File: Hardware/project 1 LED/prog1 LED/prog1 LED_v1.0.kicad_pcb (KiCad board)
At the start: 2 copper layers, 16.2 x 22 mm, 6 parts, among them J1 Conn_01x02, SW1 SW_Push

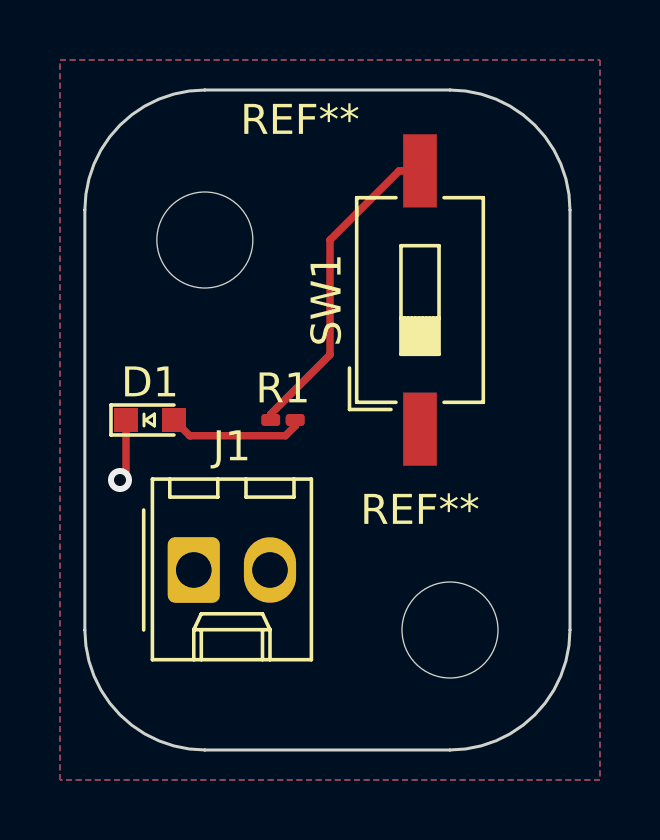
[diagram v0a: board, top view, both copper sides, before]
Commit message: finished specs for horn project
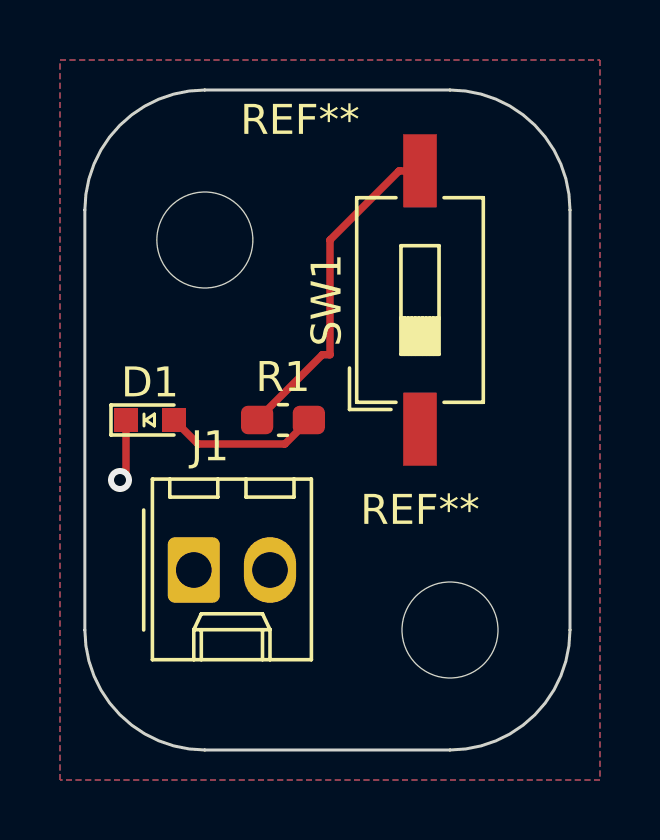
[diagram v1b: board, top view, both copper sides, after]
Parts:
- R1: footprint Resistor_SMD:R_0201_0603Metric_Pad0.64x0.40mm_HandSolder -> Capacitor_SMD:C_0603_1608Metric_Pad1.08x0.95mm_HandSolder
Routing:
- net Net-(D1-A): track 4.59 -> 5.16 mm
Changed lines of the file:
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@@
 		(tags "connector Molex KK-254 vertical")
 		(property "Reference" "J1"
-			(at 1.27 -4.12 0)
+			(at 0.54 -4.12 0)
 			(layer "F.SilkS")
 			(effects
@@
 		)
 	)
-	(footprint "Resistor_SMD:R_0201_0603Metric_Pad0.64x0.40mm_HandSolder"
+	(footprint "Capacitor_SMD:C_0603_1608Metric_Pad1.08x0.95mm_HandSolder"
 		(layer "F.Cu")
 		(at 100.4325 91)
-		(descr "Resistor SMD 0201 (0603 Metric), square (rectangular) end terminal, IPC_7351 nominal with elongated pad for handsoldering. (Body size source: https://www.vishay.com/docs/20052/crcw0201e3.pdf), generated with kicad-footprint-generator")
-		(tags "resistor handsolder")
+		(descr "Capacitor SMD 0603 (1608 Metric), square (rectangular) end terminal, IPC_7351 nominal with elongated pad for handsoldering. (Body size source: IPC-SM-782 page 76, https://www.pcb-3d.com/wordpress/wp-content/uploads/ipc-sm-782a_amendment_1_and_2.pdf), generated with kicad-footprint-generator")
+		(tags "capacitor handsolder")
 		(property "Reference" "R1"
-			(at 0 -1.05 0)
+			(at 0 -1.43 0)
 			(layer "F.SilkS")
 			(effects
@@
 		)
 		(property "Value" "105"
-			(at 0 1.05 0)
-			(layer "F.Fab")
-			(effects
-				(font
-					(size 1 1)
-					(thickness 0.15)
-				)
-			)
-		)
-		(property "Footprint" "Resistor_SMD:R_0201_0603Metric_Pad0.64x0.40mm_HandSolder"
+			(at 0 1.43 0)
+			(layer "F.Fab")
+			(effects
+				(font
+					(size 1 1)
+					(thickness 0.15)
+				)
+			)
+		)
+		(property "Footprint" "Capacitor_SMD:C_0603_1608Metric_Pad1.08x0.95mm_HandSolder"
 			(at 0 0 0)
 			(layer "F.Fab")
@@
 		(attr smd)
 		(fp_line
-			(start -0.88 -0.35)
-			(end 0.88 -0.35)
+			(start -0.146267 -0.51)
+			(end 0.146267 -0.51)
+			(stroke
+				(width 0.12)
+				(type solid)
+			)
+			(layer "F.SilkS")
+		)
+		(fp_line
+			(start -0.146267 0.51)
+			(end 0.146267 0.51)
+			(stroke
+				(width 0.12)
+				(type solid)
+			)
+			(layer "F.SilkS")
+		)
+		(fp_line
+			(start -1.65 -0.73)
+			(end 1.65 -0.73)
 			(stroke
 				(width 0.05)
@@
 		)
 		(fp_line
-			(start -0.88 0.35)
-			(end -0.88 -0.35)
+			(start -1.65 0.73)
+			(end -1.65 -0.73)
 			(stroke
 				(width 0.05)
@@
 		)
 		(fp_line
-			(start 0.88 -0.35)
-			(end 0.88 0.35)
+			(start 1.65 -0.73)
+			(end 1.65 0.73)
 			(stroke
 				(width 0.05)
@@
 		)
 		(fp_line
-			(start 0.88 0.35)
-			(end -0.88 0.35)
+			(start 1.65 0.73)
+			(end -1.65 0.73)
 			(stroke
 				(width 0.05)
@@
 		)
 		(fp_line
-			(start -0.3 -0.15)
-			(end 0.3 -0.15)
-			(stroke
-				(width 0.1)
-				(type solid)
-			)
-			(layer "F.Fab")
-		)
-		(fp_line
-			(start -0.3 0.15)
-			(end -0.3 -0.15)
-			(stroke
-				(width 0.1)
-				(type solid)
-			)
-			(layer "F.Fab")
-		)
-		(fp_line
-			(start 0.3 -0.15)
-			(end 0.3 0.15)
-			(stroke
-				(width 0.1)
-				(type solid)
-			)
-			(layer "F.Fab")
-		)
-		(fp_line
-			(start 0.3 0.15)
-			(end -0.3 0.15)
+			(start -0.8 -0.4)
+			(end 0.8 -0.4)
+			(stroke
+				(width 0.1)
+				(type solid)
+			)
+			(layer "F.Fab")
+		)
+		(fp_line
+			(start -0.8 0.4)
+			(end -0.8 -0.4)
+			(stroke
+				(width 0.1)
+				(type solid)
+			)
+			(layer "F.Fab")
+		)
+		(fp_line
+			(start 0.8 -0.4)
+			(end 0.8 0.4)
+			(stroke
+				(width 0.1)
+				(type solid)
+			)
+			(layer "F.Fab")
+		)
+		(fp_line
+			(start 0.8 0.4)
+			(end -0.8 0.4)
 			(stroke
 				(width 0.1)
@@
 		)
 		(fp_text user "${REFERENCE}"
-			(at 0 -0.68 0)
-			(layer "F.Fab")
-			(effects
-				(font
-					(size 0.25 0.25)
-					(thickness 0.04)
-				)
-			)
-		)
-		(pad "" smd roundrect
-			(at -0.4325 0)
-			(size 0.458 0.36)
-			(layers "F.Paste")
-			(roundrect_rratio 0.25)
-		)
-		(pad "" smd roundrect
-			(at 0.4325 0)
-			(size 0.458 0.36)
-			(layers "F.Paste")
-			(roundrect_rratio 0.25)
+			(at 0 0 0)
+			(layer "F.Fab")
+			(effects
+				(font
+					(size 0.4 0.4)
+					(thickness 0.06)
+				)
+			)
 		)
 		(pad "1" smd roundrect
-			(at -0.4075 0)
-			(size 0.635 0.4)
-			(layers "F.Cu" "F.Mask")
+			(at -0.8625 0)
+			(size 1.075 0.95)
+			(layers "F.Cu" "F.Paste" "F.Mask")
 			(roundrect_rratio 0.25)
 			(net 4 "Net-(R1-Pad1)")
@@
 		)
 		(pad "2" smd roundrect
-			(at 0.4075 0)
-			(size 0.635 0.4)
-			(layers "F.Cu" "F.Mask")
+			(at 0.8625 0)
+			(size 1.075 0.95)
+			(layers "F.Cu" "F.Paste" "F.Mask")
 			(roundrect_rratio 0.25)
 			(net 2 "Net-(D1-A)")
 			(pintype "passive")
 		)
-		(model "${KICAD6_3DMODEL_DIR}/Resistor_SMD.3dshapes/R_0201_0603Metric.wrl"
+		(model "${KICAD6_3DMODEL_DIR}/Capacitor_SMD.3dshapes/C_0603_1608Metric.wrl"
 			(offset
 				(xyz 0 0 0)
@@
 	)
 	(segment
-		(start 100.84 91)
-		(end 100.84 91.199999)
+		(start 100.495 91.8)
+		(end 101.295 91)
 		(width 0.25)
 		(layer "F.Cu")
@@
 	)
 	(segment
-		(start 97.325 91.525)
-		(end 96.8 91)
+		(start 97.6 91.8)
+		(end 100.495 91.8)
 		(width 0.25)
 		(layer "F.Cu")
@@
 	)
 	(segment
-		(start 100.84 91.199999)
-		(end 100.514999 91.525)
+		(start 96.8 91)
+		(end 97.6 91.8)
 		(width 0.25)
 		(layer "F.Cu")
@@
 	)
 	(segment
-		(start 100.514999 91.525)
-		(end 97.325 91.525)
-		(width 0.25)
-		(layer "F.Cu")
-		(net 2)
-	)
-	(segment
-		(start 100.025 90.800001)
-		(end 100.025 91)
-		(width 0.25)
-		(layer "F.Cu")
-		(net 4)
-	)
-	(segment
 		(start 102 88.825001)
-		(end 100.025 90.800001)
+		(end 101.744999 88.825001)
 		(width 0.25)
 		(layer "F.Cu")
@@
 		(width 0.25)
 		(layer "F.Cu")
+		(net 4)
+	)
+	(segment
+		(start 101.744999 88.825001)
+		(end 99.57 91)
+		(width 0.25)
+		(layer "F.Cu")
